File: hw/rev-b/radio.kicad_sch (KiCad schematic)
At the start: 70 parts, among them Q101 SIA975DJ-T1-GE3, Q102 2N7002, U101 TPS2116DRLR, U102 TPS2553DBVR, U103 TPS63802DLAR, U104 ESP32-C3-MINI-1U-N4, U105 SN74LVC1G125DBVR, U106 SN74LVC3G34DCUR, U107 CH334P, U108 TLV3012BIDBVR, U109 TLV431BIDBZR, Y101 12MHz 10pF 10ppm

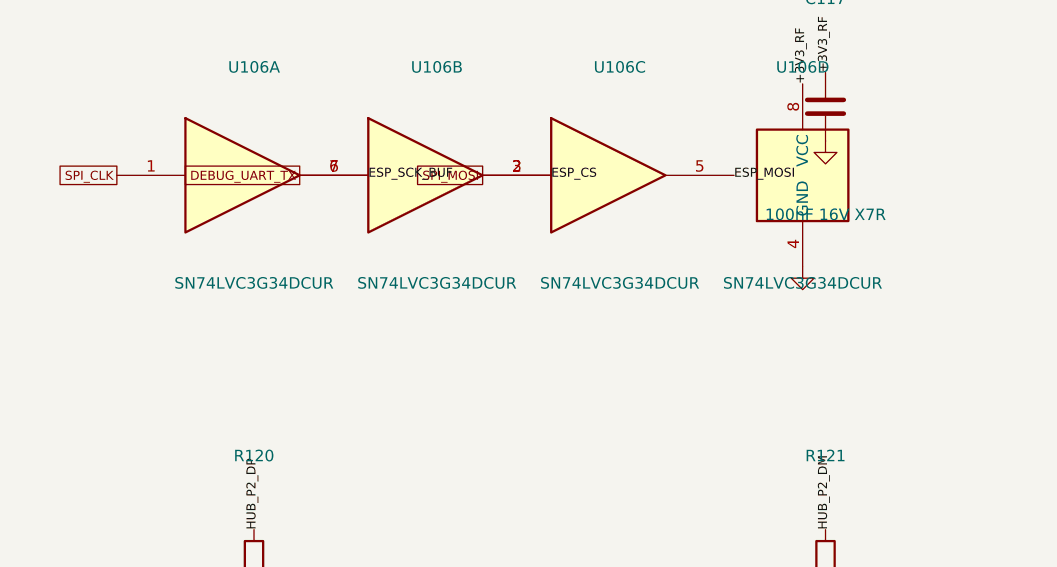
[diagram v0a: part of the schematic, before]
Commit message: board: scripted schematic->PCB update (70 footprints staged, nets, rip of USB_D_prot pair), deterministic sheet UUIDs, U106 to SM8 for clearance; parity pass; logbook
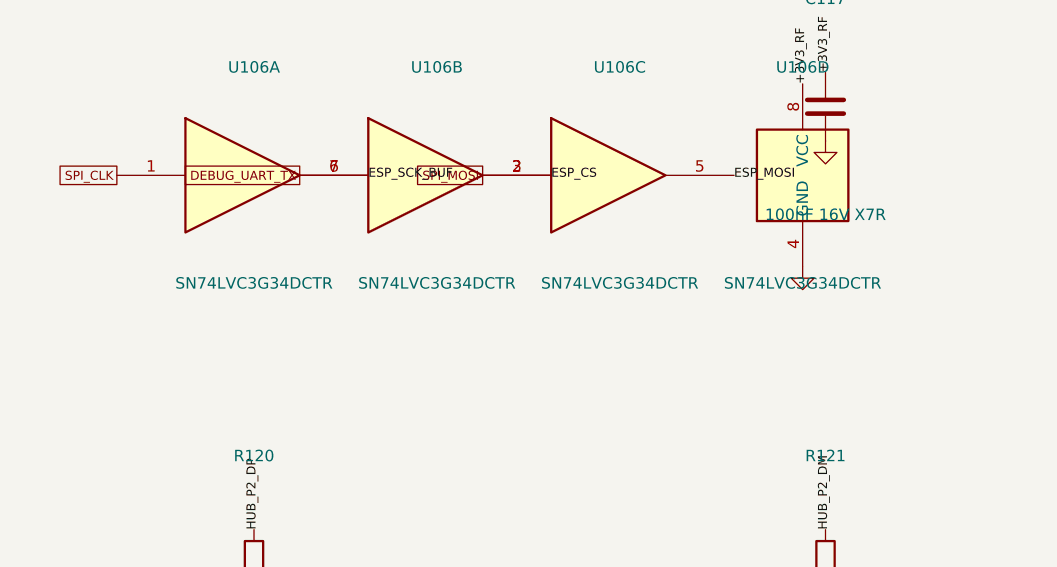
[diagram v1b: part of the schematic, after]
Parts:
- U106: value SN74LVC3G34DCUR -> SN74LVC3G34DCTR; footprint Package_SO:VSSOP-8_2.3x2mm_P0.5mm -> Package_SO:SSOP-8_2.95x2.8mm_P0.65mm; LCSC C130024 -> C139356
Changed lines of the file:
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@@
 			)
 		)
-		(property "Value" "SN74LVC3G34DCUR"
+		(property "Value" "SN74LVC3G34DCTR"
 			(at 279.4 324.42 0)
 			(effects
@@
 			)
 		)
-		(property "Footprint" "Package_SO:VSSOP-8_2.3x2mm_P0.5mm"
+		(property "Footprint" "Package_SO:SSOP-8_2.95x2.8mm_P0.65mm"
 			(at 279.4 312.42 0)
 			(effects
@@
 			)
 		)
-		(property "LCSC" "C130024"
+		(property "LCSC" "C139356"
 			(at 279.4 312.42 0)
 			(effects
@@
 			)
 		)
-		(property "Value" "SN74LVC3G34DCUR"
+		(property "Value" "SN74LVC3G34DCTR"
 			(at 299.72 324.42 0)
 			(effects
@@
 			)
 		)
-		(property "Footprint" "Package_SO:VSSOP-8_2.3x2mm_P0.5mm"
+		(property "Footprint" "Package_SO:SSOP-8_2.95x2.8mm_P0.65mm"
 			(at 299.72 312.42 0)
 			(effects
@@
 			)
 		)
-		(property "LCSC" "C130024"
+		(property "LCSC" "C139356"
 			(at 299.72 312.42 0)
 			(effects
@@
 			)
 		)
-		(property "Value" "SN74LVC3G34DCUR"
+		(property "Value" "SN74LVC3G34DCTR"
 			(at 320.04 324.42 0)
 			(effects
@@
 			)
 		)
-		(property "Footprint" "Package_SO:VSSOP-8_2.3x2mm_P0.5mm"
+		(property "Footprint" "Package_SO:SSOP-8_2.95x2.8mm_P0.65mm"
 			(at 320.04 312.42 0)
 			(effects
@@
 			)
 		)
-		(property "LCSC" "C130024"
+		(property "LCSC" "C139356"
 			(at 320.04 312.42 0)
 			(effects
@@
 			)
 		)
-		(property "Value" "SN74LVC3G34DCUR"
+		(property "Value" "SN74LVC3G34DCTR"
 			(at 340.36 324.42 0)
 			(effects
@@
 			)
 		)
-		(property "Footprint" "Package_SO:VSSOP-8_2.3x2mm_P0.5mm"
+		(property "Footprint" "Package_SO:SSOP-8_2.95x2.8mm_P0.65mm"
 			(at 340.36 312.42 0)
 			(effects
@@
 			)
 		)
-		(property "LCSC" "C130024"
+		(property "LCSC" "C139356"
 			(at 340.36 312.42 0)
 			(effects

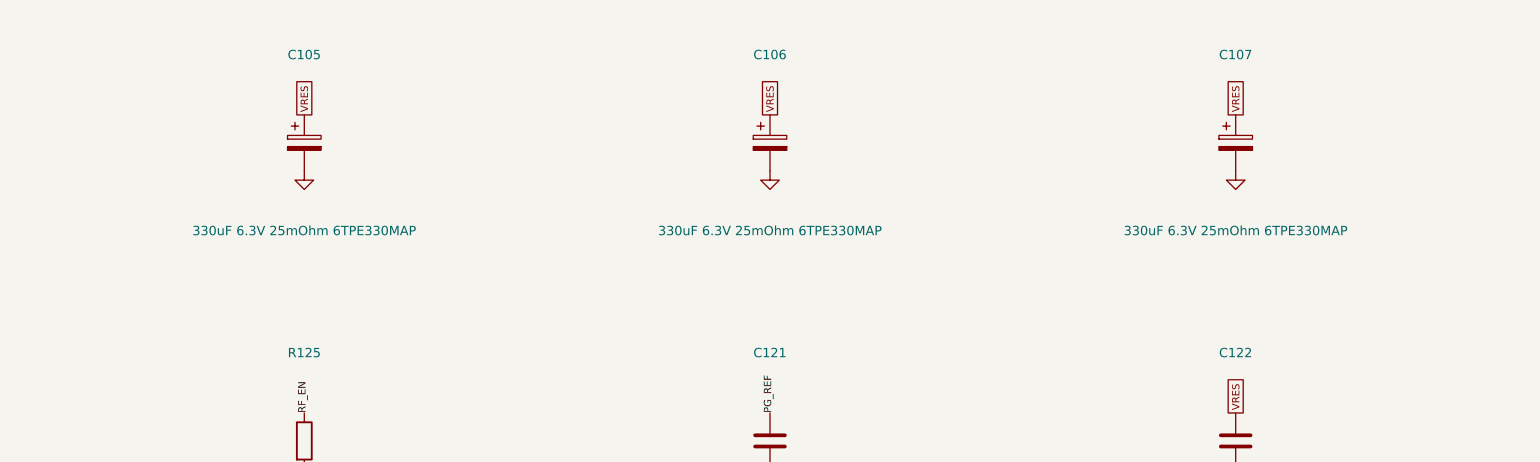
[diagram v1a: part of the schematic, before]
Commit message: T520B reservoir (audits A1-A8 pass at -20% C), sim: firmware vs actual reservoir C, footprint swap in update_pcb, autoplace tool (result rejected, reverted), logbook
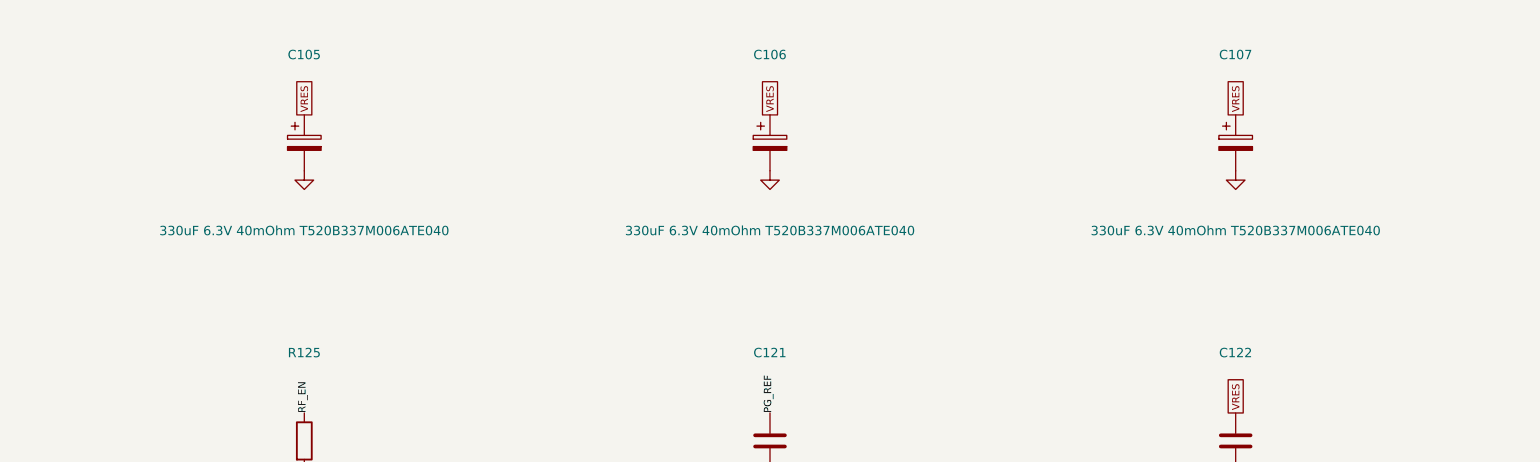
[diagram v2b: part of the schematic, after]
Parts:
- C105, C106, C107: value 330uF 6.3V 25mOhm 6TPE330MAP -> 330uF 6.3V 40mOhm T520B337M006ATE040; footprint Capacitor_Tantalum_SMD:CP_EIA-7343-20_Kemet-V -> Capacitor_Tantalum_SMD:CP_EIA-3528-21_Kemet-B; LCSC C79112 -> C696806
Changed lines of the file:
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@@
 			)
 		)
-		(property "Value" "330uF 6.3V 25mOhm 6TPE330MAP"
+		(property "Value" "330uF 6.3V 40mOhm T520B337M006ATE040"
 			(at 215.9 103.44 0)
 			(effects
@@
 			)
 		)
-		(property "Footprint" "Capacitor_Tantalum_SMD:CP_EIA-7343-20_Kemet-V"
+		(property "Footprint" "Capacitor_Tantalum_SMD:CP_EIA-3528-21_Kemet-B"
 			(at 215.9 91.44 0)
 			(effects
@@
 			)
 		)
-		(property "Datasheet" ""
+		(property "Datasheet" "https://wmsc.lcsc.com/wmsc/upload/file/pdf/v2/lcsc/2304140030_KEMET-T520B337M006ATE040_C696806.pdf"
 			(at 215.9 91.44 0)
 			(effects
@@
 			)
 		)
-		(property "LCSC" "C79112"
+		(property "LCSC" "C696806"
 			(at 215.9 91.44 0)
 			(effects
@@
 			)
 		)
-		(property "Value" "330uF 6.3V 25mOhm 6TPE330MAP"
+		(property "Value" "330uF 6.3V 40mOhm T520B337M006ATE040"
 			(at 279.4 103.44 0)
 			(effects
@@
 			)
 		)
-		(property "Footprint" "Capacitor_Tantalum_SMD:CP_EIA-7343-20_Kemet-V"
+		(property "Footprint" "Capacitor_Tantalum_SMD:CP_EIA-3528-21_Kemet-B"
 			(at 279.4 91.44 0)
 			(effects
@@
 			)
 		)
-		(property "Datasheet" ""
+		(property "Datasheet" "https://wmsc.lcsc.com/wmsc/upload/file/pdf/v2/lcsc/2304140030_KEMET-T520B337M006ATE040_C696806.pdf"
 			(at 279.4 91.44 0)
 			(effects
@@
 			)
 		)
-		(property "LCSC" "C79112"
+		(property "LCSC" "C696806"
 			(at 279.4 91.44 0)
 			(effects
@@
 			)
 		)
-		(property "Value" "330uF 6.3V 25mOhm 6TPE330MAP"
+		(property "Value" "330uF 6.3V 40mOhm T520B337M006ATE040"
 			(at 342.9 103.44 0)
 			(effects
@@
 			)
 		)
-		(property "Footprint" "Capacitor_Tantalum_SMD:CP_EIA-7343-20_Kemet-V"
+		(property "Footprint" "Capacitor_Tantalum_SMD:CP_EIA-3528-21_Kemet-B"
 			(at 342.9 91.44 0)
 			(effects
@@
 			)
 		)
-		(property "Datasheet" ""
+		(property "Datasheet" "https://wmsc.lcsc.com/wmsc/upload/file/pdf/v2/lcsc/2304140030_KEMET-T520B337M006ATE040_C696806.pdf"
 			(at 342.9 91.44 0)
 			(effects
@@
 			)
 		)
-		(property "LCSC" "C79112"
+		(property "LCSC" "C696806"
 			(at 342.9 91.44 0)
 			(effects

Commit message: option A area check: does not fit; SOD-523 clamp diodes; geometry plot tools; logbook
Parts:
- D101, D102, D103, D104: value 1N4148WS -> 1N4148WT; footprint Diode_SMD:D_SOD-323 -> Diode_SMD:D_SOD-523; LCSC C2128 -> C27748
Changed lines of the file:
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@@
 			)
 		)
-		(property "Value" "1N4148WS"
+		(property "Value" "1N4148WT"
 			(at 406.4 403.16 0)
 			(effects
@@
 			)
 		)
-		(property "Footprint" "Diode_SMD:D_SOD-323"
+		(property "Footprint" "Diode_SMD:D_SOD-523"
 			(at 406.4 391.16 0)
 			(effects
@@
 			)
 		)
-		(property "LCSC" "C2128"
+		(property "LCSC" "C27748"
 			(at 406.4 391.16 0)
 			(effects
@@
 			)
 		)
-		(property "Value" "1N4148WS"
+		(property "Value" "1N4148WT"
 			(at 469.9 403.16 0)
 			(effects
@@
 			)
 		)
-		(property "Footprint" "Diode_SMD:D_SOD-323"
+		(property "Footprint" "Diode_SMD:D_SOD-523"
 			(at 469.9 391.16 0)
 			(effects
@@
 			)
 		)
-		(property "LCSC" "C2128"
+		(property "LCSC" "C27748"
 			(at 469.9 391.16 0)
 			(effects
@@
 			)
 		)
-		(property "Value" "1N4148WS"
+		(property "Value" "1N4148WT"
 			(at 25.4 441.26 0)
 			(effects
@@
 			)
 		)
-		(property "Footprint" "Diode_SMD:D_SOD-323"
+		(property "Footprint" "Diode_SMD:D_SOD-523"
 			(at 25.4 429.26 0)
 			(effects
@@
 			)
 		)
-		(property "LCSC" "C2128"
+		(property "LCSC" "C27748"
 			(at 25.4 429.26 0)
 			(effects
@@
 			)
 		)
-		(property "Value" "1N4148WS"
+		(property "Value" "1N4148WT"
 			(at 215.9 441.26 0)
 			(effects
@@
 			)
 		)
-		(property "Footprint" "Diode_SMD:D_SOD-323"
+		(property "Footprint" "Diode_SMD:D_SOD-523"
 			(at 215.9 429.26 0)
 			(effects
@@
 			)
 		)
-		(property "LCSC" "C2128"
+		(property "LCSC" "C27748"
 			(at 215.9 429.26 0)
 			(effects

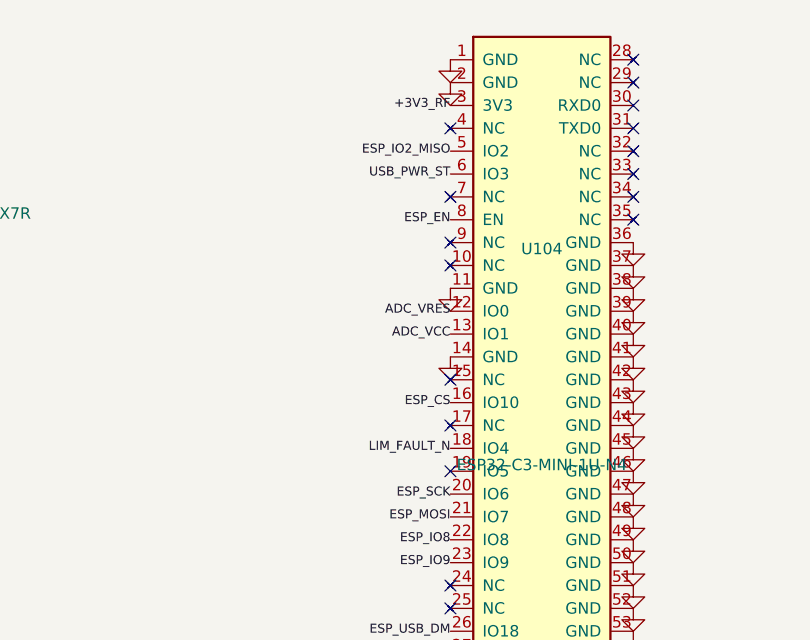
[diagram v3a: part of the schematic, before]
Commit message: routing WIP: FB/PG resistor block re-arranged, USB_PWR_ST moved to ESP IO5 (pin 19), ADC_VCC divider moved to the VCC source; 5 open
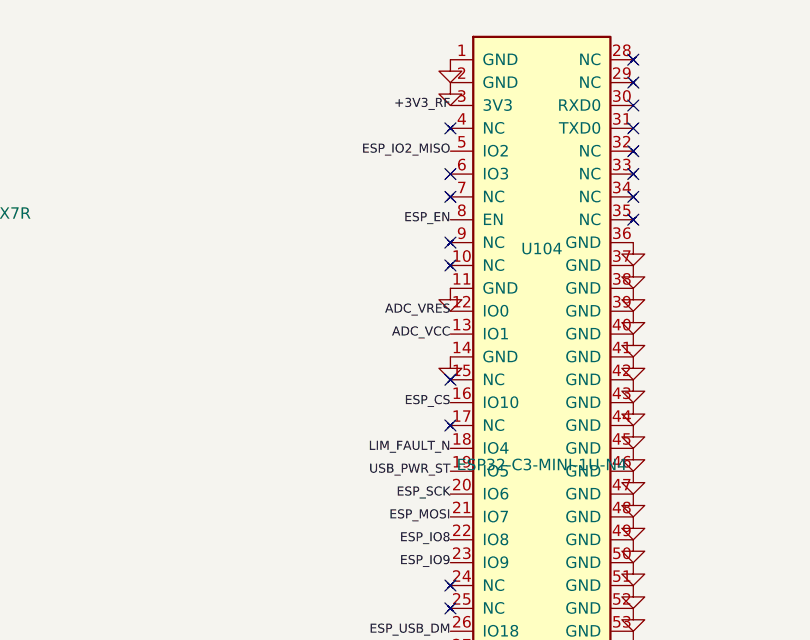
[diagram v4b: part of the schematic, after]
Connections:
- net USB_PWR_ST: now also U104.19 (IO5); no longer U104.6 (IO3)
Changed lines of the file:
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@@
 		)
 	)
-	(label "USB_PWR_ST"
-		(at 396.24 180.34 180)
-		(fields_autoplaced yes)
-		(effects
-			(font
-				(size 1.0 1.0)
-			)
-			(justify right)
-		)
+	(no_connect
+		(at 396.24 180.34)
 	)
 	(no_connect
@@
 		)
 	)
-	(no_connect
-		(at 396.24 213.36)
+	(label "USB_PWR_ST"
+		(at 396.24 213.36 180)
+		(fields_autoplaced yes)
+		(effects
+			(font
+				(size 1.0 1.0)
+			)
+			(justify right)
+		)
 	)
 	(label "ESP_SCK"
